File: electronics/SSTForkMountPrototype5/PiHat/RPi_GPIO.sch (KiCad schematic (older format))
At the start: 1 part, among them J2 RPi_GPIO

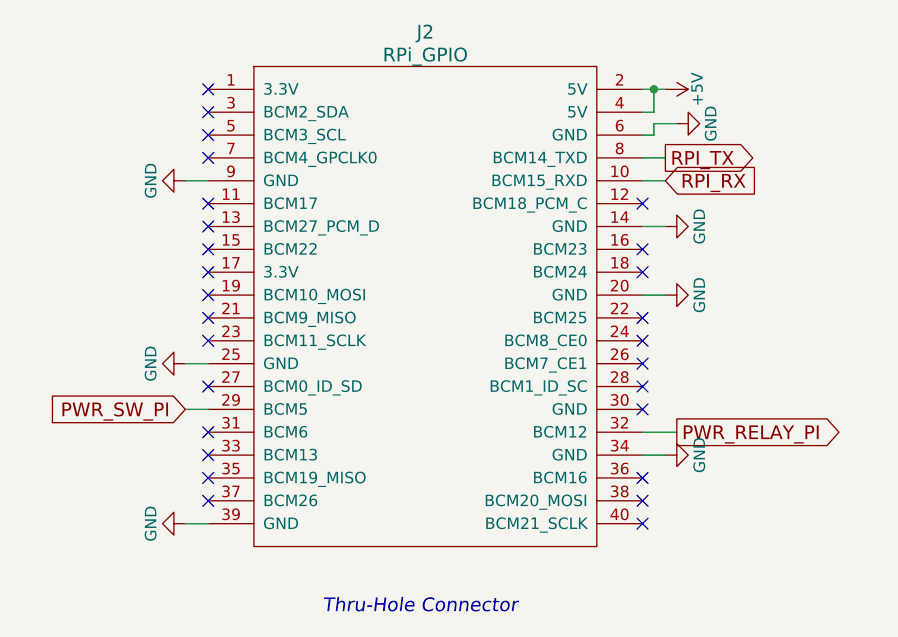
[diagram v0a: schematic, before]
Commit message: Removed mosfet switching. Seperate DEC/RA encoder headers.
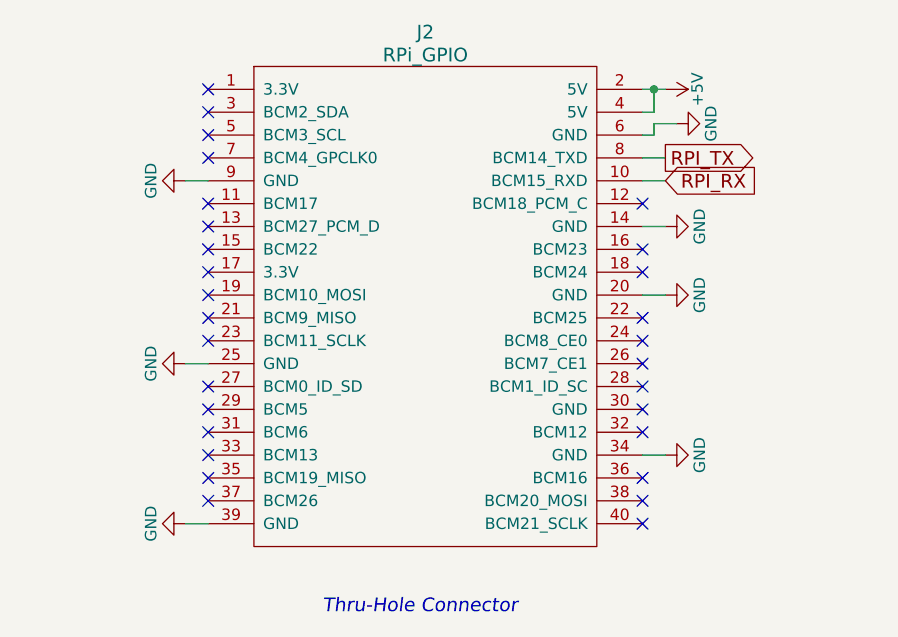
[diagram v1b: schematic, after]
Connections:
- net PWR_RELAY_PI: no longer names the net of J2.32 (BCM12)
- net PWR_SW_PI: no longer names the net of J2.29 (BCM5)
- no-connect marks 27 -> 29
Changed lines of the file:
@@
 NoConn ~ 7300 2800
 NoConn ~ 7300 2700
-Text GLabel 7200 4100 0    60   Input ~ 0
-PWR_SW_PI
-Wire Wire Line
-	7200 4100 7300 4100
-Text GLabel 9350 4200 2    60   Output ~ 0
-PWR_RELAY_PI
 Wire Wire Line
 	9250 2700 9300 2700
-Wire Wire Line
-	9200 4200 9350 4200
 NoConn ~ 7300 4200
+NoConn ~ 9200 4200
+NoConn ~ 7300 4100
 $EndSCHEMATC
